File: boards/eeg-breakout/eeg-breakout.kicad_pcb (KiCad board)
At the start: 4 copper layers, 18 x 36.5 mm, 36 parts, among them J1 Isolated SPI, J2 Electrodes, U1 ISOW7741, U2 ADS1292IRSMR

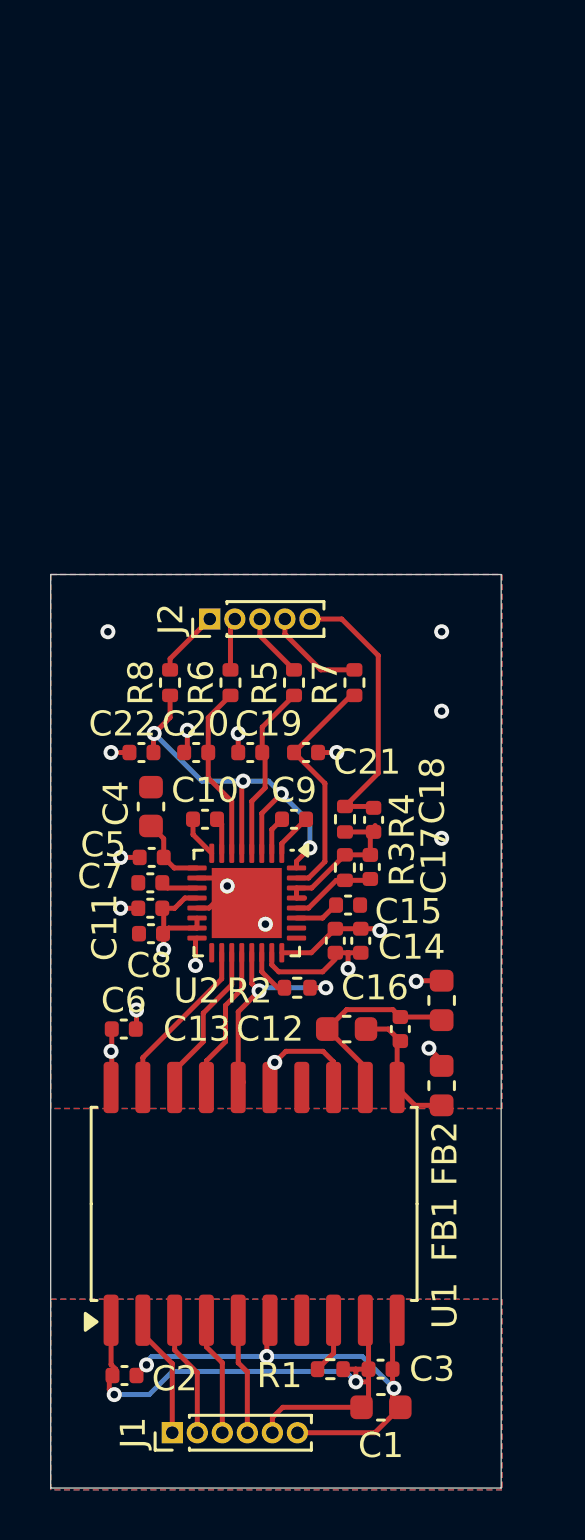
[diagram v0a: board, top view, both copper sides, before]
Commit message: feat: tweak the eeg breakout
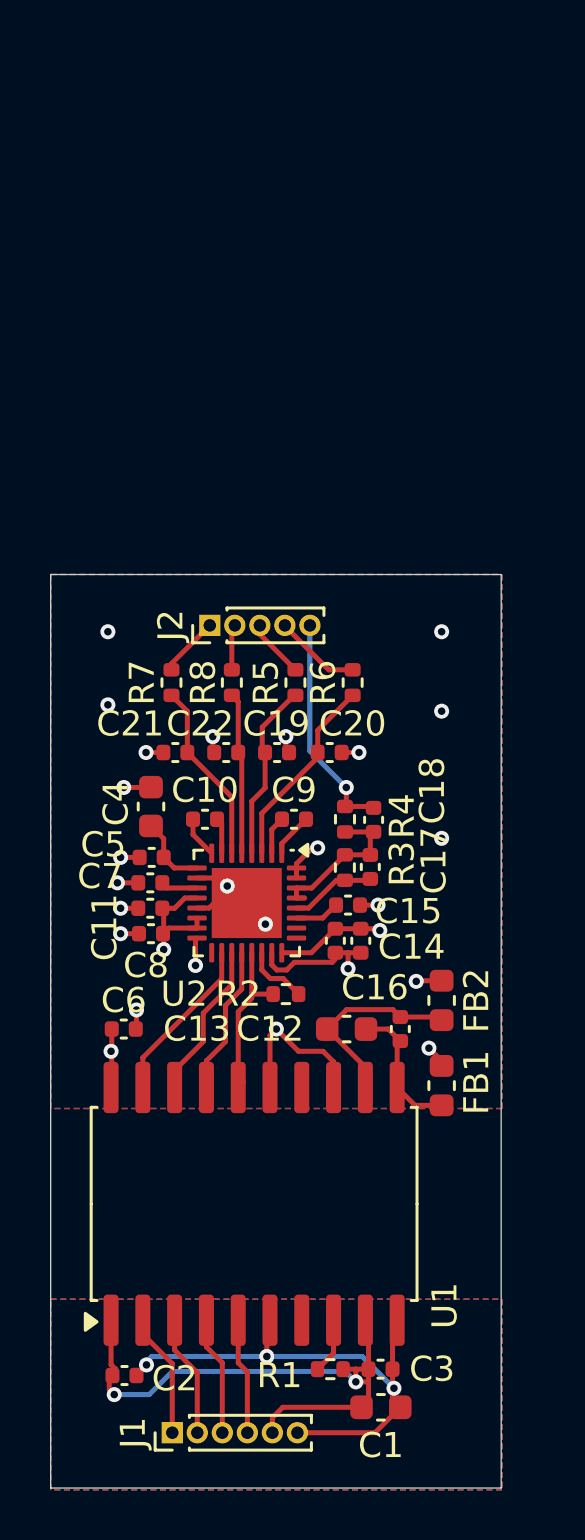
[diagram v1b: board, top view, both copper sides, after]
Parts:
- C17: value 1.5n -> 1n
- moved R7 7.31 mm to (19.1, 163.3)
- moved C20 5.33 mm to (25.4, 166.1), turned to 0 degrees
- moved C21 5.22 mm to (19.2, 166.1), turned to 180 degrees
- moved R6 4.88 mm to (26.3, 163.3)
- moved C22 3.39 mm to (21.2, 166.1)
- moved R8 2.47 mm to (21.5, 163.3)
- moved C19 1.07 mm to (23.3, 166.1), turned to 0 degrees
- moved R2 0.52 mm to (23.6, 175.8), turned to 180 degrees
- moved J2 0.25 mm to (20.6, 161.0)
- moved R5 0.06 mm to (24.0, 163.3)
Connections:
- net /EEG_BIAS renamed /BIAS
- net /EEG_F4 renamed /CH1_P
- C20 pad 1: /IN2P -> /IN1N
- C21 pad 1: /IN3P -> /IN2P
- C22 pad 1: /IN1N -> /IN2N
- J2 pad 1: /EEG_M1 -> /CH2_P
- J2 pad 2: /EEG_C4 -> /CH2_N
- J2 pad 4: /EEG_O2 -> /CH1_N
- R6 pad 1: /IN2P -> /IN1N
- R6 pad 2: /EEG_C4 -> /CH1_N
- R7 pad 1: /IN3P -> /IN2P
- R7 pad 2: /EEG_O2 -> /CH2_P
- R8 pad 1: /IN1N -> /IN2N
- R8 pad 2: /EEG_M1 -> /CH2_N
- U2 pad 31: /IN3P -> +3V3
- U2 pad 32: /IN1N -> +3V3
- U2 pad 5: /IN1N -> /IN2N
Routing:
- net /IN1N: track 17.9 -> 7.95 mm, vias 4 -> 0
- net /IN3P: track 9.64 -> 0.00 mm
- net /IN2N: track 0.00 -> 6.47 mm
- net GND: track 19.7 -> 24.1 mm, vias 17 -> 22
- net /EEG_O2: track 3.97 -> 0.00 mm
- net /CH1_N: track 0.00 -> 3.46 mm
- net /ISO_DOUT/~{DRDY}: track 9.51 -> 6.77 mm, vias 2 -> 0
- net /EEG_M1: track 2.69 -> 0.00 mm
- net /CH2_P: track 0.00 -> 2.41 mm
- net /EEG_C4: track 2.10 -> 0.00 mm
- net /CH2_N: track 0.00 -> 2.07 mm
- net /BIAS: track 11.1 -> 9.28 mm, vias 0 -> 1
- net +3V3: track 15.1 -> 16.9 mm, vias 4 -> 5
- net Net-(U2-~{DRDY}): track 1.93 -> 2.56 mm

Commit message: refactor: improve ads1292 breakout
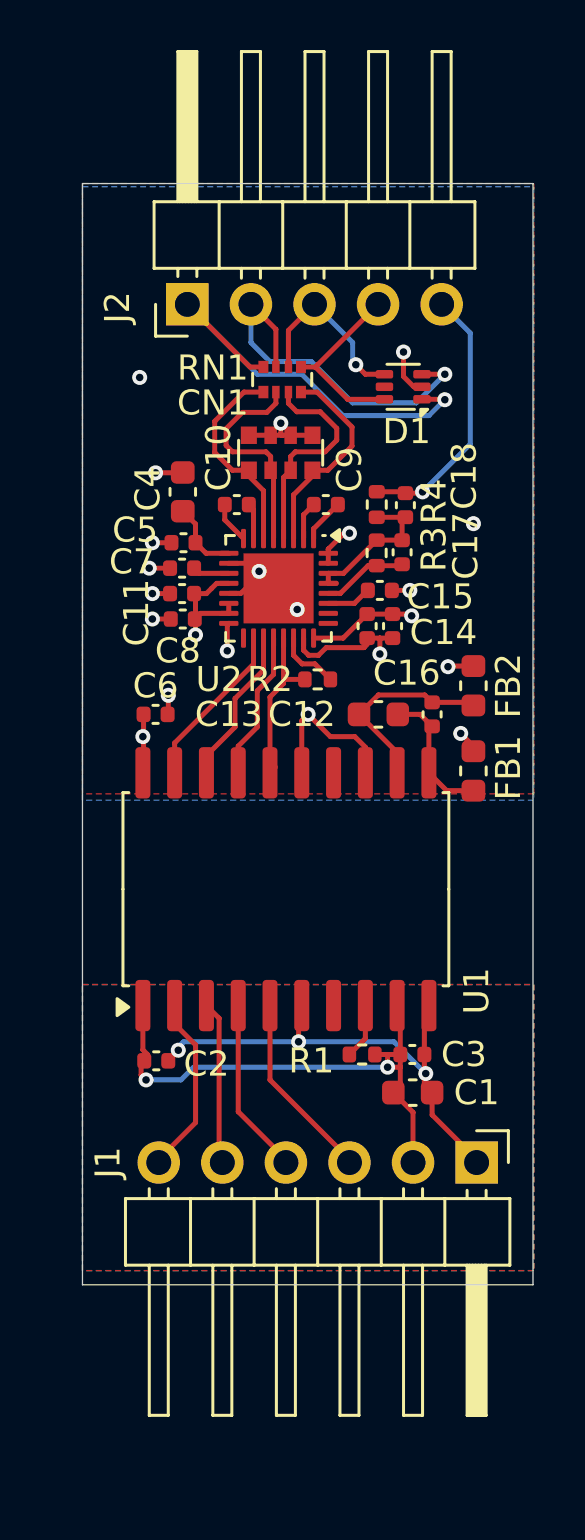
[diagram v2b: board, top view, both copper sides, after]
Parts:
- removed C19, C20, C21, C22: 1n, Capacitor_SMD:C_0402_1005Metric
- removed R5, R6, R7, R8: 2.2k, Resistor_SMD:R_0402_1005Metric
- added CN1: 1n, Resistor_SMD:R_Array_Convex_4x0612, F.Cu at (23.4, 154.1)
- added D1: TPD4E1B06DRLR, Package_TO_SOT_SMD:SOT-563, F.Cu at (28.3, 151.5)
- added RN1: 2.2k, Resistor_SMD:R_Array_Convex_4x0402, F.Cu at (23.5, 151.2)
- J1: footprint Connector_PinHeader_1.00mm:PinHeader_1x06_P1.00mm_Vertical -> Connector_PinHeader_2.54mm:PinHeader_1x06_P2.54mm_Horizontal
- J2: footprint Connector_PinHeader_1.00mm:PinHeader_1x05_P1.00mm_Vertical -> Connector_PinHeader_2.54mm:PinHeader_1x05_P2.54mm_Horizontal
- R1, R2: value 4.7k -> 10k
- moved J1 16.3 mm to (31.2, 182.5), turned to -90 degrees
- moved J2 12.9 mm to (19.7, 148.2)
- moved C11 12.6 mm to (19.5, 159.8)
- moved C14 12.6 mm to (27.9, 161.1)
- moved C16 12.6 mm to (26.9, 161.1)
- moved C2 12.6 mm to (18.4, 178.4)
- moved C4 12.6 mm to (19.5, 155.7)
- moved C7 12.6 mm to (19.5, 158.8)
- moved FB1 12.6 mm to (31.1, 166.9)
- moved R2 12.6 mm to (24.9, 163.2)
- moved R3 12.6 mm to (27.2, 158.1)
- moved R4 12.6 mm to (27.3, 156.2)
- moved U1 12.6 mm to (23.6, 171.6)
- moved U2 12.6 mm to (23.3, 159.6)
- moved C1 12.6 mm to (28.7, 179.7)
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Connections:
- net /BIAS renamed /ELEC_BIAS
- J1 pad 1: /~{CS} -> /VSS
- J1 pad 2: /DIN -> /VDD
- J1 pad 3: /SCLK -> /DOUT/~{DRDY}
- J1 pad 4: /DOUT/~{DRDY} -> /SCLK
- J1 pad 5: /VDD -> /DIN
- J1 pad 6: /VSS -> /~{CS}
- J2 pad 1: /CH2_P -> /ELEC_2P
- J2 pad 2: /CH2_N -> /ELEC_2N
- J2 pad 3: /CH1_P -> /ELEC_1P
- J2 pad 4: /CH1_N -> /ELEC_1N
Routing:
- net /ELEC_2P: track 0.00 -> 17.4 mm, vias 0 -> 1
- net /ELEC_2N: track 0.00 -> 14.6 mm, vias 0 -> 1
- net /ELEC_1N: track 0.00 -> 7.41 mm
- net /ELEC_1P: track 0.00 -> 7.33 mm, vias 0 -> 1
- net /CH1_N: track 3.46 -> 0.00 mm
- net /DOUT/~{DRDY}: track 4.65 -> 7.46 mm
- net /CH2_P: track 2.41 -> 0.00 mm
- net /CH1_P: track 2.36 -> 0.00 mm
- net /IN2N: track 6.47 -> 8.82 mm
- net GND: track 24.1 -> 26.3 mm, vias 22 -> 17
- net /SCLK: track 4.76 -> 6.93 mm
- net /~{CS}: track 4.98 -> 7.10 mm
- net /CH2_N: track 2.07 -> 0.00 mm
- net /VDD: track 23.1 -> 21.5 mm
- net /IN1P: track 7.10 -> 8.78 mm
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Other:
- board size 18 x 36.5 mm -> 18 x 44 mm
